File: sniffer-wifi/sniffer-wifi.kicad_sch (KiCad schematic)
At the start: 67 parts, among them J1 USB_B_Micro, J2 Conn_01x05_Socket, J3 Screw_Terminal_01x02, J4 Screw_Terminal_01x02, J5 Conn_02x04_Odd_Even, Q1 MMBT3904, Q2 MMBT3904, Q5 MMBT3904, Q6 MMBT5551L, U1 AMS1117-3.3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

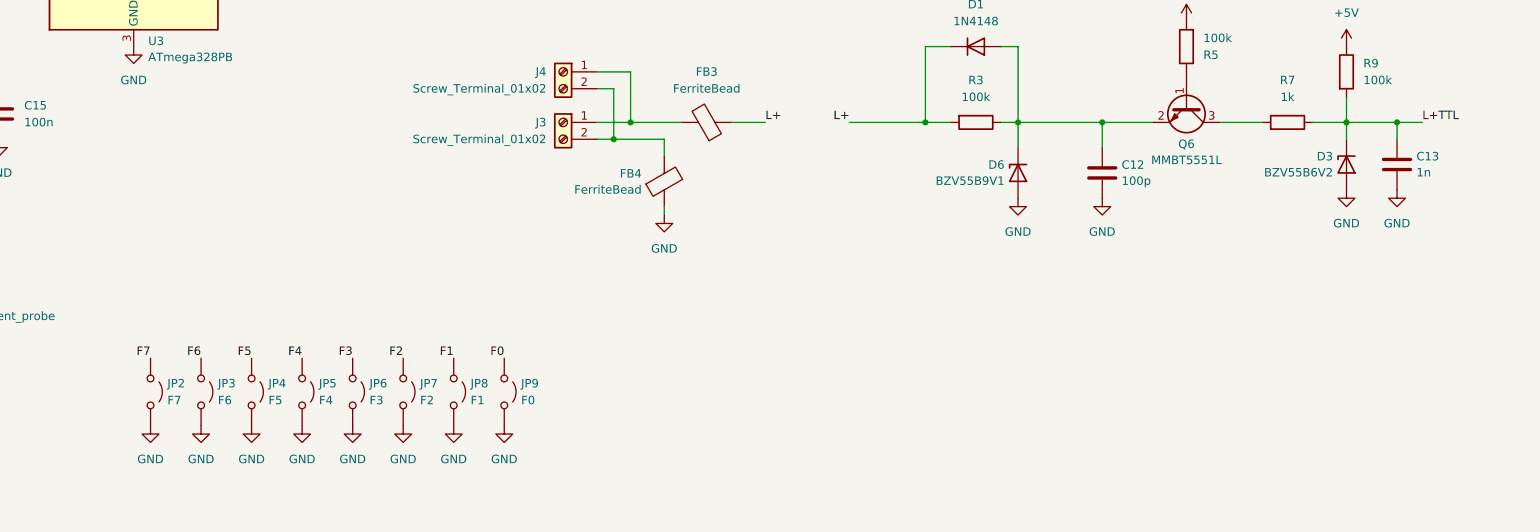
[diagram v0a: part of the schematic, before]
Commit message: update capacitors, replace jumpers with pin header
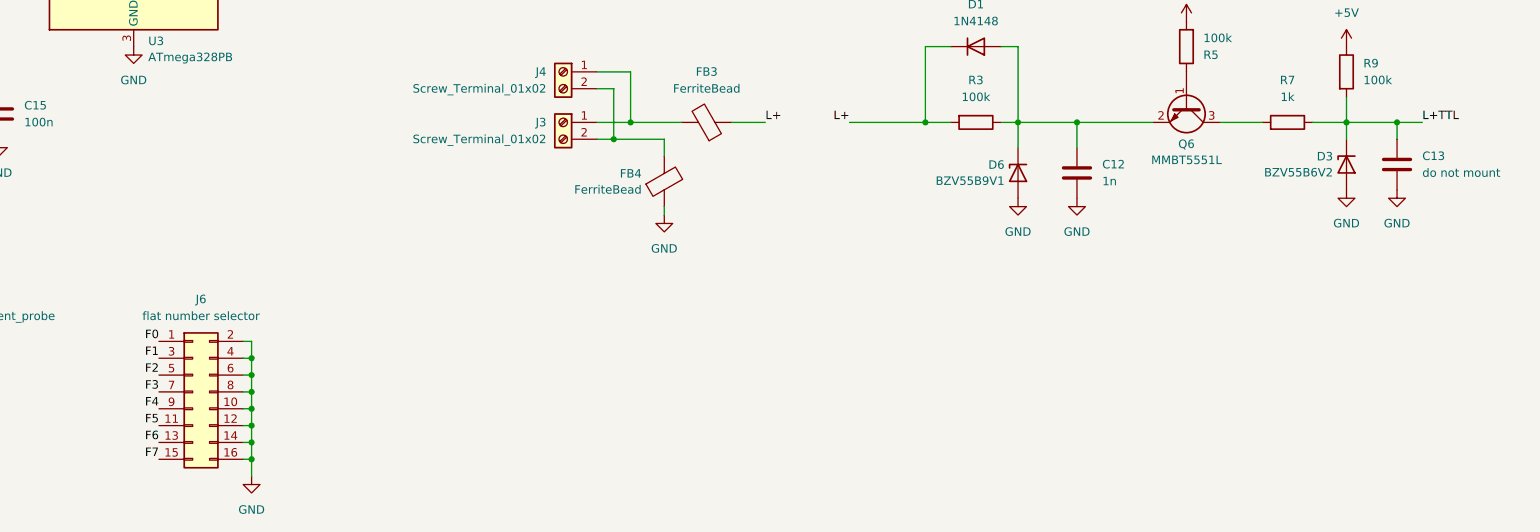
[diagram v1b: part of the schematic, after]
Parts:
- removed JP2: F7, symbol Jumper:Jumper_2_Open
- removed JP3: F6, symbol Jumper:Jumper_2_Open
- removed JP4: F5, symbol Jumper:Jumper_2_Open
- removed JP5: F4, symbol Jumper:Jumper_2_Open
- removed JP6: F3, symbol Jumper:Jumper_2_Open
- removed JP7: F2, symbol Jumper:Jumper_2_Open
- removed JP8: F1, symbol Jumper:Jumper_2_Open
- removed JP9: F0, symbol Jumper:Jumper_2_Open
- added J6: flat number selector, Connector_IDC:IDC-Header_2x08_P2.54mm_Latch_Vertical, symbol Connector_Generic:Conn_02x08_Odd_Even
- C12: value 100p -> 1n
- C13: value 1n -> do not mount
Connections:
- net F0: now also J6.1 (Pin_1)
- net F1: now also J6.3 (Pin_3)
- net F2: now also J6.5 (Pin_5)
- net F3: now also J6.7 (Pin_7)
- net F4: now also J6.9 (Pin_9)
- net F5: now also J6.11 (Pin_11)
- net F6: now also J6.13 (Pin_13)
- net F7: now also J6.15 (Pin_15)
- net GND: now also J6.10 (Pin_10), J6.12 (Pin_12), J6.14 (Pin_14), J6.16 (Pin_16), J6.2 (Pin_2), J6.4 (Pin_4), J6.6 (Pin_6), J6.8 (Pin_8)
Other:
- moved on the sheet: C12

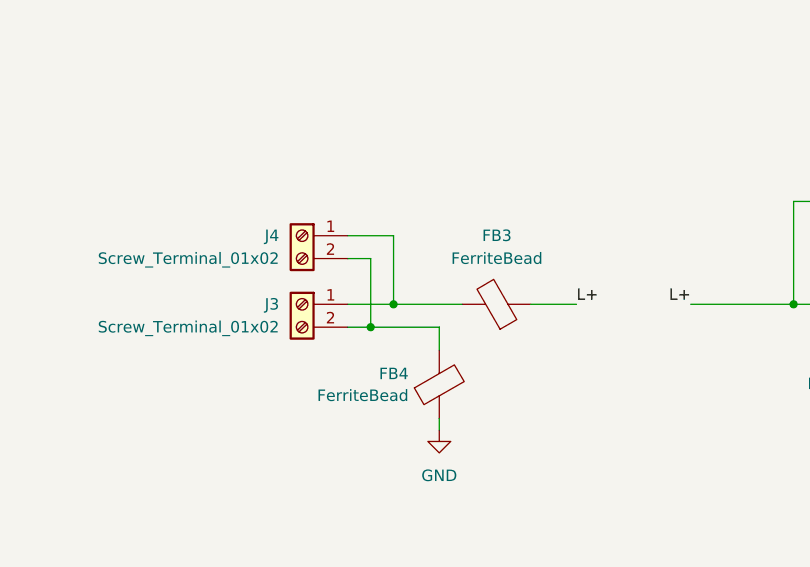
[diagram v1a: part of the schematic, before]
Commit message: switch terminals in an ARK connector
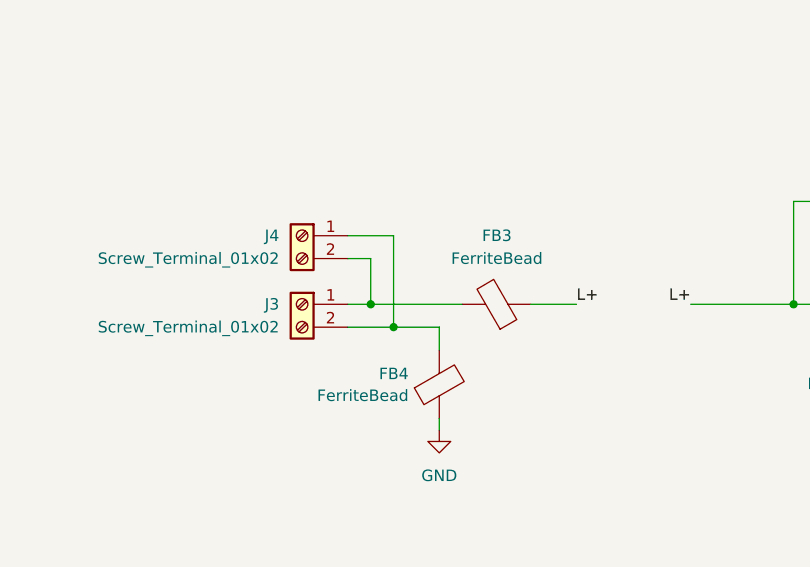
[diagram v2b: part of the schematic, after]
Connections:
- net at FB3.2, J3.1 (Pin_1): now also J4.2 (Pin_2); no longer J4.1 (Pin_1)
- net at FB4.2, J3.2 (Pin_2): now also J4.1 (Pin_1); no longer J4.2 (Pin_2)
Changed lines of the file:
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@@
+	)
+	(junction
+		(at 148.59 133.35)
+		(diameter 0)
+		(color 0 0 0 0)
 	)
 	(junction
@@
 	)
 	(junction
-		(at 151.13 133.35)
-		(diameter 0)
-		(color 0 0 0 0)
-	)
-	(junction
 		(at 261.62 77.47)
 		(diameter 0)
@@
 	)
 	(junction
-		(at 148.59 135.89)
-		(diameter 0)
-		(color 0 0 0 0)
-	)
-	(junction
 		(at 93.98 176.53)
 		(diameter 0)
@@
 	(junction
 		(at 195.58 133.35)
+		(diameter 0)
+		(color 0 0 0 0)
+	)
+	(junction
+		(at 151.13 135.89)
 		(diameter 0)
 		(color 0 0 0 0)
@@
 	(wire
 		(pts
-			(xy 151.13 125.73) (xy 151.13 133.35)
-		)
-		(stroke
-			(width 0)
-			(type default)
-		)
-	)
-	(wire
-		(pts
 			(xy 195.58 121.92) (xy 195.58 133.35)
 		)
@@
 	(wire
 		(pts
-			(xy 151.13 133.35) (xy 146.05 133.35)
-		)
-		(stroke
-			(width 0)
-			(type default)
-		)
-	)
-	(wire
-		(pts
 			(xy 92.71 181.61) (xy 93.98 181.61)
 		)
@@
 	(wire
 		(pts
+			(xy 148.59 128.27) (xy 148.59 133.35)
+		)
+		(stroke
+			(width 0)
+			(type default)
+		)
+	)
+	(wire
+		(pts
 			(xy 261.62 77.47) (xy 261.62 78.74)
 		)
@@
 	(wire
 		(pts
-			(xy 156.21 135.89) (xy 148.59 135.89)
+			(xy 146.05 135.89) (xy 151.13 135.89)
 		)
 		(stroke
@@
 	(wire
 		(pts
-			(xy 148.59 135.89) (xy 146.05 135.89)
-		)
-		(stroke
-			(width 0)
-			(type default)
-		)
-	)
-	(wire
-		(pts
 			(xy 92.71 171.45) (xy 93.98 171.45)
 		)
@@
 	(wire
 		(pts
-			(xy 148.59 128.27) (xy 148.59 135.89)
-		)
-		(stroke
-			(width 0)
-			(type default)
-		)
-	)
-	(wire
-		(pts
 			(xy 33.02 135.89) (xy 33.02 134.62)
 		)
@@
 	(wire
 		(pts
-			(xy 158.75 133.35) (xy 151.13 133.35)
+			(xy 146.05 133.35) (xy 148.59 133.35)
 		)
 		(stroke
@@
 	(wire
 		(pts
+			(xy 151.13 125.73) (xy 151.13 135.89)
+		)
+		(stroke
+			(width 0)
+			(type default)
+		)
+	)
+	(wire
+		(pts
 			(xy 20.32 125.73) (xy 20.32 127)
 		)
@@
 	(wire
 		(pts
+			(xy 151.13 135.89) (xy 156.21 135.89)
+		)
+		(stroke
+			(width 0)
+			(type default)
+		)
+	)
+	(wire
+		(pts
 			(xy 266.7 133.35) (xy 270.51 133.35)
 		)
@@
 		)
 		(stroke
+			(width 0)
+			(type default)
+		)
+	)
+	(wire
+		(pts
+			(xy 148.59 133.35) (xy 158.75 133.35)
+		)
+		(stroke
